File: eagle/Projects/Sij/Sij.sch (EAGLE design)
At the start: 9 parts, among them U1 ATMEGA2560AU

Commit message: ajouté des pièces pour digikey
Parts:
- added U2: BQ76925_PW_20, TI:BQ76925_PW_20
- added U3: LM1085_KTT_3, TI:LM1085_KTT_3
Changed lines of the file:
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@@
 <part name="C2" library="SparkFun-Capacitors" deviceset="22PF-50V-5%(0603)" device="" value="20pF"/>
 <part name="GND2" library="SparkFun-Aesthetics" deviceset="GND" device=""/>
+<part name="U2" library="TI" deviceset="BQ76925_PW_20" device=""/>
+<part name="U3" library="TI" deviceset="LM1085_KTT_3" device=""/>
 </parts>
 <sheets>
@@
 <instance part="C2" gate="G$1" x="-38.1" y="121.92" rot="R90"/>
 <instance part="GND2" gate="1" x="-58.42" y="109.22"/>
+<instance part="U2" gate="A" x="246.38" y="132.08"/>
+<instance part="U3" gate="A" x="233.68" y="68.58"/>
 </instances>
 <busses>

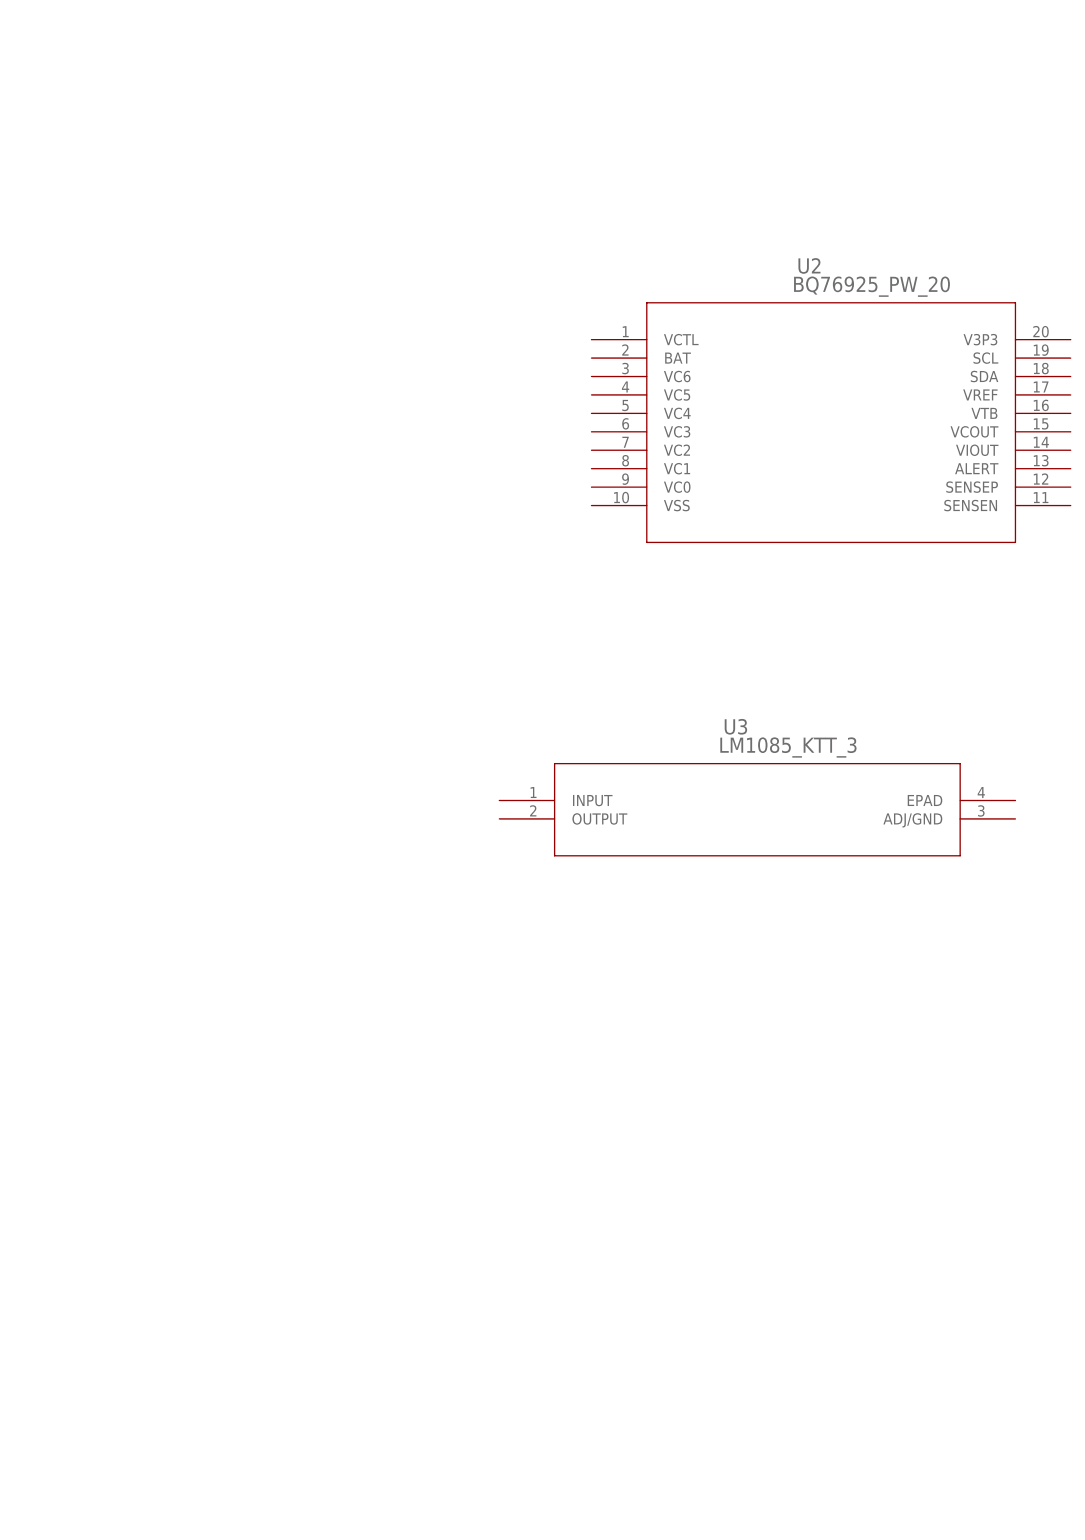
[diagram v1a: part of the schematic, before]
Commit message: ajouté des bibliothèques de composantes, modifié beaucoup le schematic du pcb et ajouté des listes d'épicerie
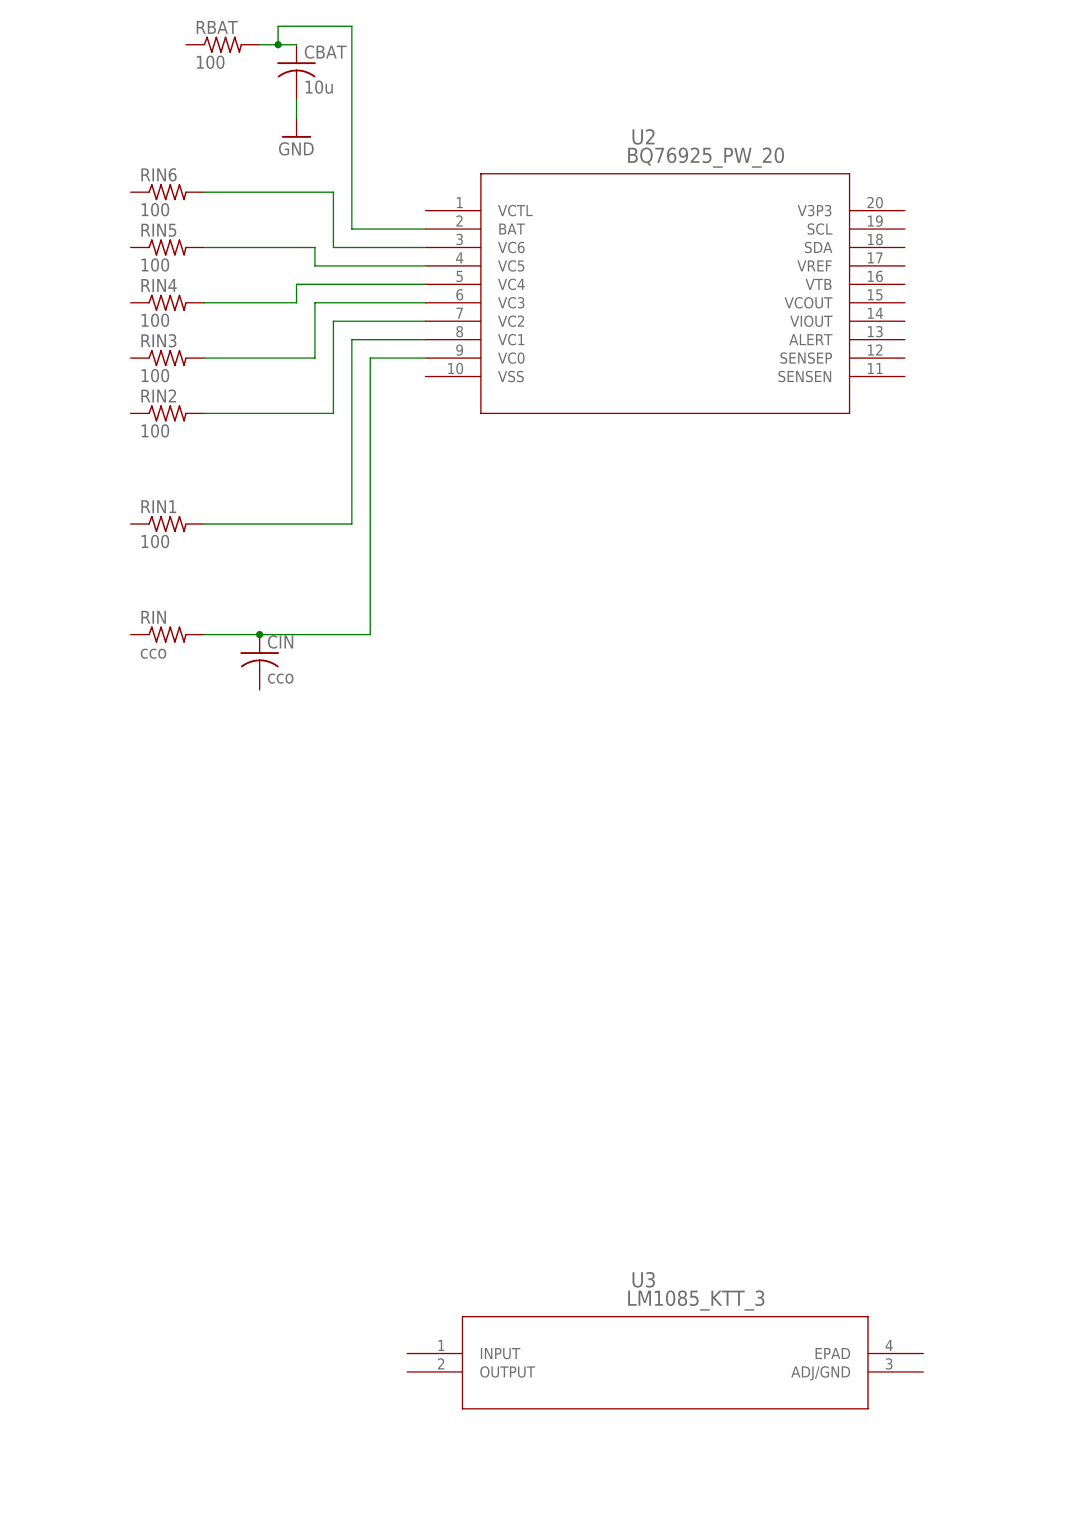
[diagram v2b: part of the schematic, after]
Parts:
- added CBAT: 10u, rcl:C-USC0805
- added CIN: cco, rcl:C-USC0805
- added RBAT, RIN1, RIN2, RIN3, RIN4, RIN5, RIN6: 100, rcl:R-US_R0805
- added RIN: cco, rcl:R-US_R0805
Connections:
- new net N$10: RIN1.2, U2.VC1
- new net N$11: CIN.1, RIN.2, U2.VC0
- new net N$12: RIN4.2, U2.VC4
- new net N$17: RIN6.2, U2.VC6
- new net N$18: RIN5.2, U2.VC5
- new net N$7: RIN3.2, U2.VC3
- new net N$8: CBAT.1, RBAT.2, U2.BAT
- new net N$9: RIN2.2, U2.VC2
- net GND: now also CBAT.2
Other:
- moved on the sheet: U2, U3
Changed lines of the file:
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@@
 <part name="U2" library="TI" deviceset="BQ76925_PW_20" device=""/>
 <part name="U3" library="TI" deviceset="LM1085_KTT_3" device=""/>
+<part name="RBAT" library="rcl" deviceset="R-US_" device="R0805" value="100"/>
+<part name="RIN" library="rcl" deviceset="R-US_" device="R0805" value="cco"/>
+<part name="CBAT" library="rcl" deviceset="C-US" device="C0805" value="10u"/>
+<part name="GND3" library="SparkFun-Aesthetics" deviceset="GND" device=""/>
+<part name="RIN1" library="rcl" deviceset="R-US_" device="R0805" value="100"/>
+<part name="RIN2" library="rcl" deviceset="R-US_" device="R0805" value="100"/>
+<part name="RIN3" library="rcl" deviceset="R-US_" device="R0805" value="100"/>
+<part name="RIN4" library="rcl" deviceset="R-US_" device="R0805" value="100"/>
+<part name="RIN5" library="rcl" deviceset="R-US_" device="R0805" value="100"/>
+<part name="RIN6" library="rcl" deviceset="R-US_" device="R0805" value="100"/>
+<part name="CIN" library="rcl" deviceset="C-US" device="C0805" value="cco"/>
 </parts>
 <sheets>
@@
 <instance part="C2" gate="G$1" x="-38.1" y="121.92" rot="R90"/>
 <instance part="GND2" gate="1" x="-58.42" y="109.22"/>
-<instance part="U2" gate="A" x="246.38" y="132.08"/>
-<instance part="U3" gate="A" x="233.68" y="68.58"/>
+<instance part="U2" gate="A" x="223.52" y="149.86"/>
+<instance part="U3" gate="A" x="220.98" y="-7.62"/>
+<instance part="RBAT" gate="G$1" x="195.58" y="172.72"/>
+<instance part="RIN" gate="G$1" x="187.96" y="91.44"/>
+<instance part="CBAT" gate="G$1" x="205.74" y="170.18"/>
+<instance part="GND3" gate="1" x="205.74" y="160.02"/>
+<instance part="RIN1" gate="G$1" x="187.96" y="106.68"/>
+<instance part="RIN2" gate="G$1" x="187.96" y="121.92"/>
+<instance part="RIN3" gate="G$1" x="187.96" y="129.54"/>
+<instance part="RIN4" gate="G$1" x="187.96" y="137.16"/>
+<instance part="RIN5" gate="G$1" x="187.96" y="144.78"/>
+<instance part="RIN6" gate="G$1" x="187.96" y="152.4"/>
+<instance part="CIN" gate="G$1" x="200.66" y="88.9"/>
 </instances>
 <busses>
@@
 <junction x="-50.8" y="116.84"/>
 </segment>
+<segment>
+<pinref part="GND3" gate="1" pin="GND"/>
+<pinref part="CBAT" gate="G$1" pin="2"/>
+<wire x1="205.74" y1="162.56" x2="205.74" y2="165.1" width="0.1524" layer="91"/>
+</segment>
 </net>
 <net name="VCC" class="0">
@@
 </segment>
 </net>
+<net name="N$8" class="0">
+<segment>
+<pinref part="RBAT" gate="G$1" pin="2"/>
+<pinref part="CBAT" gate="G$1" pin="1"/>
+<wire x1="205.74" y1="172.72" x2="203.2" y2="172.72" width="0.1524" layer="91"/>
+<pinref part="U2" gate="A" pin="BAT"/>
+<wire x1="203.2" y1="172.72" x2="200.66" y2="172.72" width="0.1524" layer="91"/>
+<wire x1="223.52" y1="147.32" x2="213.36" y2="147.32" width="0.1524" layer="91"/>
+<wire x1="213.36" y1="147.32" x2="213.36" y2="175.26" width="0.1524" layer="91"/>
+<wire x1="213.36" y1="175.26" x2="203.2" y2="175.26" width="0.1524" layer="91"/>
+<wire x1="203.2" y1="175.26" x2="203.2" y2="172.72" width="0.1524" layer="91"/>
+<junction x="203.2" y="172.72"/>
+</segment>
+</net>
+<net name="N$17" class="0">
+<segment>
+<pinref part="U2" gate="A" pin="VC6"/>
+<wire x1="223.52" y1="144.78" x2="210.82" y2="144.78" width="0.1524" layer="91"/>
+<wire x1="210.82" y1="144.78" x2="210.82" y2="152.4" width="0.1524" layer="91"/>
+<pinref part="RIN6" gate="G$1" pin="2"/>
+<wire x1="210.82" y1="152.4" x2="193.04" y2="152.4" width="0.1524" layer="91"/>
+</segment>
+</net>
+<net name="N$18" class="0">
+<segment>
+<pinref part="U2" gate="A" pin="VC5"/>
+<wire x1="223.52" y1="142.24" x2="208.28" y2="142.24" width="0.1524" layer="91"/>
+<wire x1="208.28" y1="142.24" x2="208.28" y2="144.78" width="0.1524" layer="91"/>
+<pinref part="RIN5" gate="G$1" pin="2"/>
+<wire x1="208.28" y1="144.78" x2="193.04" y2="144.78" width="0.1524" layer="91"/>
+</segment>
+</net>
+<net name="N$7" class="0">
+<segment>
+<pinref part="U2" gate="A" pin="VC3"/>
+<wire x1="223.52" y1="137.16" x2="208.28" y2="137.16" width="0.1524" layer="91"/>
+<wire x1="208.28" y1="137.16" x2="208.28" y2="129.54" width="0.1524" layer="91"/>
+<pinref part="RIN3" gate="G$1" pin="2"/>
+<wire x1="208.28" y1="129.54" x2="193.04" y2="129.54" width="0.1524" layer="91"/>
+</segment>
+</net>
+<net name="N$9" class="0">
+<segment>
+<pinref part="U2" gate="A" pin="VC2"/>
+<wire x1="223.52" y1="134.62" x2="210.82" y2="134.62" width="0.1524" layer="91"/>
+<wire x1="210.82" y1="134.62" x2="210.82" y2="121.92" width="0.1524" layer="91"/>
+<pinref part="RIN2" gate="G$1" pin="2"/>
+<wire x1="210.82" y1="121.92" x2="193.04" y2="121.92" width="0.1524" layer="91"/>
+</segment>
+</net>
+<net name="N$10" class="0">
+<segment>
+<pinref part="U2" gate="A" pin="VC1"/>
+<wire x1="223.52" y1="132.08" x2="213.36" y2="132.08" width="0.1524" layer="91"/>
+<wire x1="213.36" y1="132.08" x2="213.36" y2="106.68" width="0.1524" layer="91"/>
+<pinref part="RIN1" gate="G$1" pin="2"/>
+<wire x1="213.36" y1="106.68" x2="193.04" y2="106.68" width="0.1524" layer="91"/>
+</segment>
+</net>
+<net name="N$11" class="0">
+<segment>
+<pinref part="U2" gate="A" pin="VC0"/>
+<wire x1="223.52" y1="129.54" x2="215.9" y2="129.54" width="0.1524" layer="91"/>
+<wire x1="215.9" y1="129.54" x2="215.9" y2="91.44" width="0.1524" layer="91"/>
+<pinref part="RIN" gate="G$1" pin="2"/>
+<wire x1="215.9" y1="91.44" x2="200.66" y2="91.44" width="0.1524" layer="91"/>
+<pinref part="CIN" gate="G$1" pin="1"/>
+<wire x1="200.66" y1="91.44" x2="193.04" y2="91.44" width="0.1524" layer="91"/>
+<junction x="200.66" y="91.44"/>
+</segment>
+</net>
+<net name="N$12" class="0">
+<segment>
+<pinref part="U2" gate="A" pin="VC4"/>
+<wire x1="223.52" y1="139.7" x2="205.74" y2="139.7" width="0.1524" layer="91"/>
+<wire x1="205.74" y1="139.7" x2="205.74" y2="137.16" width="0.1524" layer="91"/>
+<pinref part="RIN4" gate="G$1" pin="2"/>
+<wire x1="205.74" y1="137.16" x2="193.04" y2="137.16" width="0.1524" layer="91"/>
+</segment>
+</net>

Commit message: modifié le TODO
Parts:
- added BAT+, BAT-: AWG_10_HOLE_PAD, custom_parts:AWG_10_HOLE_PAD
- added CIN1, CIN2, CIN3, CIN4, CIN5, CIN6, COUT2, CREF: 1.0uF, SparkFun-Capacitors:1.0UF-16V-10%(0603)
- added CIN_1085: 10uF, SparkFun-Capacitors:22UF-6.3V-20%(0805)
- added CIN_7805: 0.22uF, SparkFun-Capacitors:0.22UF-25V-10%(0603)
- added COUT: 0.1u, SparkFun-Capacitors:CAP0603-CAP
- added COUT_1085: 10uF, SparkFun-Capacitors:CAP1206
- added COUT_7805: 0.1uF, SparkFun-Capacitors:0.1UF-25V-5%(0603)
- added CSENSE: 0.1u, rcl:C-USC0805
- added CV3P3: 4.7uF, SparkFun-Capacitors:4.7UF-6.3V-10%(0603)0603
- added ESC1+, ESC1-, ESC2+, ESC2-, ESC3+, ESC3-, ESC4+, ESC4-: BULLET_PAD, custom_parts:BULLET_PAD
- added ESC1_PWM, ESC2_PWM, ESC3_PWM, ESC4_PWM, JUMP_3_CELL, JUMP_4_CELL, JUMP_5_CELL, JUMP_PWR_BAT, JUMP_PWR_PROG: (no value), SparkFun-Connectors:M02PTH
- added J1: (no value), SparkFun-Connectors:M06FEMALE_LOCK
- added R1: 121, resistor:R-US_R0603
- added R2: adj, resistor:R-US_R0603
- added RSENSE: 1m, resistor:R-US_R1206
- added RSENSEN, RSENSEP: 1K, resistor:R-US_R0603
- added U$1: 7_PIN_JST-XH, JST-XH_HEADERS:7_PIN_JST-XH
- added U4: LM7805, TI:LM7805
- CBAT: value 10u -> 10uF; device rcl:C-USC0805 -> SparkFun-Capacitors:CAP0805
- CIN: value cco -> 1.0uF; device rcl:C-USC0805 -> SparkFun-Capacitors:1.0UF-16V-10%(0603)
- RBAT, RIN1, RIN2, RIN3, RIN4, RIN5, RIN6: device rcl:R-US_R0805 -> resistor:R-US_R0603
- RIN: value cco -> 100; device rcl:R-US_R0805 -> resistor:R-US_R0603
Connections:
- new net GND-ISO: ESC1-.PAD, ESC2-.PAD, ESC3-.PAD, ESC4-.PAD, RSENSE.1, RSENSEN.1
- new net N$13: COUT_7805.1, JUMP_PWR_BAT.2, U4.OUT
- new net N$14: BAT-.0, RSENSE.2, RSENSEP.1
- new net N$15: CSENSE.1, RSENSEN.2, U2.SENSEN
- new net N$16: CSENSE.2, RSENSEP.2, U2.SENSEP
- new net N$19: U2.SDA
- new net N$20: U2.ALERT
- new net N$21: COUT2.1, U2.VIOUT
- new net N$22: COUT.1, U2.VCOUT
- new net N$23: RIN1.1, U$1.P$2
- new net N$24: CREF.1, U2.VREF
- new net N$25: U2.SCL
- new net N$26: CV3P3.1, U2.V3P3
- new net N$27: RIN2.1, U$1.P$3
- new net N$28: JUMP_3_CELL.1, RIN3.1, U$1.P$4
- new net N$29: JUMP_3_CELL.2, JUMP_4_CELL.1, RIN4.1, U$1.P$5
- new net N$30: JUMP_4_CELL.2, JUMP_5_CELL.1, RIN5.1, U$1.P$6
- new net N$31: ICSP.2, JUMP_PWR_PROG.1
- new net N$32: COUT_1085.1, J1.1, J1.2, J1.3, J1.4, J1.5, J1.6, R1.1, U3.EPAD, U3.OUTPUT
- new net N$33: R1.2, R2.2, U3.ADJ/GND
- new net V_BATT: BAT+.0, CIN_1085.1, CIN_7805.1, ESC1+.PAD, ESC2+.PAD, ESC3+.PAD, ESC4+.PAD, JUMP_5_CELL.2, RBAT.1, RIN6.1, U$1.P$7, U3.INPUT, U4.IN
- net GND: now also CIN.2, CIN1.2, CIN2.2, CIN3.2, CIN4.2, CIN5.2, CIN6.2, CIN_1085.2, CIN_7805.2, COUT.2, COUT2.2, COUT_1085.2, COUT_7805.2, CREF.2, CV3P3.2, ESC1_PWM.2, ESC2_PWM.2, ESC3_PWM.2, ESC4_PWM.2, R2.1, RIN.1, U$1.P$1, U1.GND, U1.GND1, U1.GND2, U1.GND3, U2.VSS, U4.GND
- net N$10: now also CIN1.1
- net N$12: now also CIN4.1
- net N$17: now also CIN6.1
- net N$18: now also CIN5.1
- net N$7: now also CIN3.1
- net N$8: now also U2.VCTL
- net N$9: now also CIN2.1
- net PWMH1: now also ESC1_PWM.1, ESC4_PWM.1, U1.PH6(OC2B)
- net PWMH2: now also ESC3_PWM.1
- net PWMH3: now also ESC2_PWM.1
- net PWMH4: no longer U1.PH6(OC2B)
- net VCC: now also JUMP_PWR_BAT.1, JUMP_PWR_PROG.2, U1.VCC, U1.VCC1, U1.VCC2, U1.VCC3; no longer ICSP.2
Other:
- note added: "Battery"
- note added: "ESC"
- note added: "More 5V supply 3A"
- note added: "Need pull up resistors to VDD"
- note added: "Power"
- note added: "To ADC pin"
- note added: "To ADC ref voltage"
- note added: "To GPIO pin"
- note added: "buffer vide pour l'instant"
- note added: "to SCL of I2C on uC"
- note added: "to SDA of I2C on uC"
- note added: "to header for 4mA 3.3V regulated"
- moved on the sheet: CBAT, CIN, ESC3, ESC4, RBAT, RIN, RIN1, RIN2, RIN3, RIN4, RIN5, RIN6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
